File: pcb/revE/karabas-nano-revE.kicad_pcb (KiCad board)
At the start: 2 copper layers, 101.6 x 99.7 mm, 155 parts, among them J1 DC 5V, J10 PWR, J11 AVR ISP, J2 TAPE IN/OUT, J3 A/V, J4 BUS, J5 KEYBOARD, J6 BUS, J7 JTAG, J9 RGB, Q1 BC846B, SW1 RESET, SW10 8, SW11 9, SW12 0, SW13 Q, SW14 A, SW15 CS, SW16 W, SW17 S, SW18 Z, SW19 E, SW2 NMI, SW20 D, SW21 X, SW22 R, SW23 F, SW24 C, SW25 T, SW26 G, SW27 V, SW28 Y, SW29 H, SW3 1, SW30 B, SW31 U, SW32 J, SW33 N, SW34 I, SW35 K, SW36 M, SW37 O, SW38 L, SW39 SS, SW4 2, SW40 P, SW41 Enter, SW42 Space, SW5 3, SW6 4, SW7 5, SW8 6, SW9 7, U1 Z80, U13 LM1117-3.3, U2 27C512, U3 BS62LV1600, U4 ATmega8A-AU, U5 ESP-12E, U6 EPM3256ATC144, U7 MicroSD, U9 AD724, Y1 28MHz, Y3 4.43MHz, Y4 20MHz

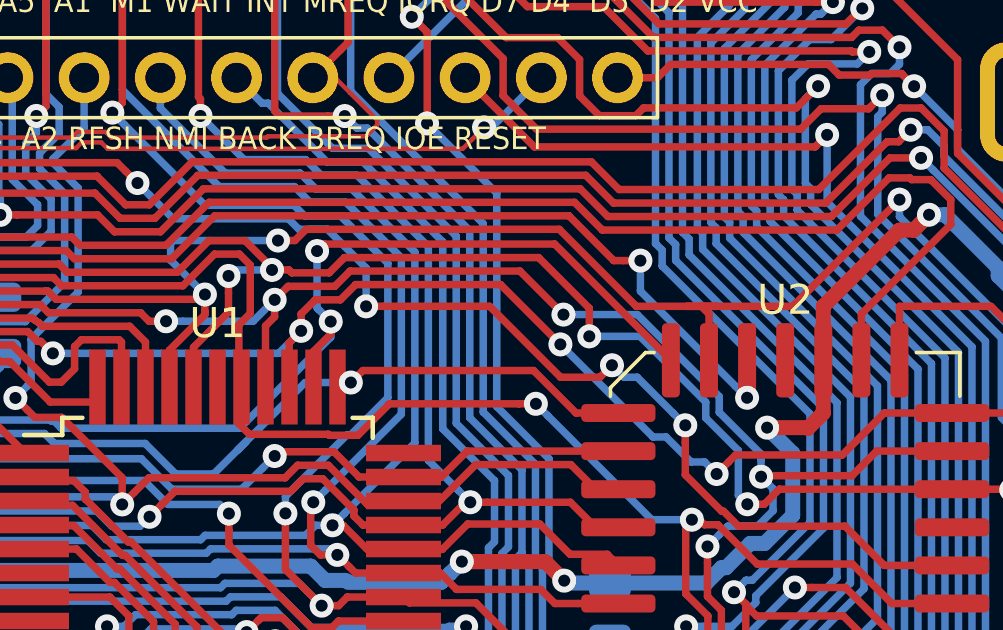
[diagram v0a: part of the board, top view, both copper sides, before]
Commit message: fixed out of sync between schematics and pcb
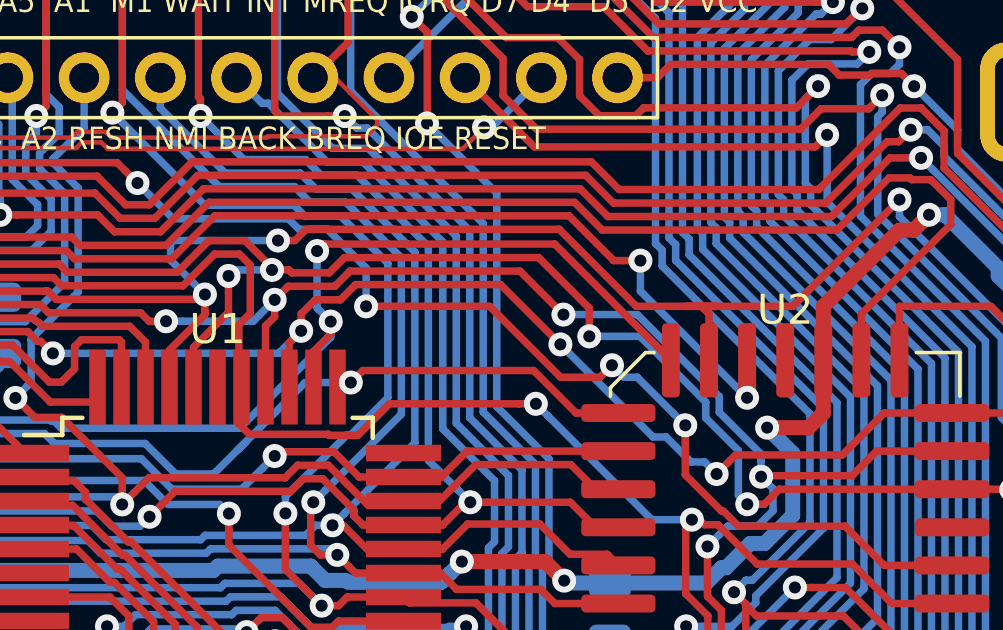
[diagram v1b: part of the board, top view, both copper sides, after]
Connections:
- SW10 pad 2: Net-(SW10-Pad2) -> /KA12
- SW10 pad 4: Net-(SW10-Pad4) -> /KB2
- SW11 pad 2: Net-(SW11-Pad2) -> /KA12
- SW11 pad 4: Net-(SW11-Pad4) -> /KB1
- SW12 pad 2: Net-(SW12-Pad2) -> /KA12
- SW12 pad 4: Net-(SW12-Pad4) -> /KB0
- SW13 pad 2: Net-(SW13-Pad2) -> /KA10
- SW13 pad 3: Net-(SW13-Pad3) -> /KB0
- SW13 pad 4: Net-(SW13-Pad4) -> /KB0
- SW14 pad 2: Net-(SW14-Pad2) -> /KA9
- SW14 pad 3: Net-(SW14-Pad3) -> /KB0
- SW14 pad 4: Net-(SW14-Pad4) -> /KB0
- SW15 pad 3: Net-(SW15-Pad3) -> /KB0
- SW15 pad 4: Net-(SW15-Pad4) -> /KB0
- SW16 pad 2: Net-(SW16-Pad2) -> /KA10
- SW16 pad 3: Net-(SW16-Pad3) -> /KB1
- SW16 pad 4: Net-(SW16-Pad4) -> /KB1
- SW17 pad 2: Net-(SW17-Pad2) -> /KA9
- SW17 pad 3: Net-(SW17-Pad3) -> /KB1
- SW17 pad 4: Net-(SW17-Pad4) -> /KB1
- SW18 pad 2: Net-(SW18-Pad2) -> /KA8
- SW18 pad 3: Net-(SW18-Pad3) -> /KB1
- SW18 pad 4: Net-(SW18-Pad4) -> /KB1
- SW19 pad 2: Net-(SW19-Pad2) -> /KA10
- SW19 pad 3: Net-(SW19-Pad3) -> /KB2
- SW19 pad 4: Net-(SW19-Pad4) -> /KB2
- SW20 pad 2: Net-(SW20-Pad2) -> /KA9
- SW20 pad 3: Net-(SW20-Pad3) -> /KB2
- SW20 pad 4: Net-(SW20-Pad4) -> /KB2
- SW21 pad 2: Net-(SW21-Pad2) -> /KA8
- SW21 pad 3: Net-(SW21-Pad3) -> /KB2
- SW21 pad 4: Net-(SW21-Pad4) -> /KB2
- SW22 pad 2: Net-(SW22-Pad2) -> /KA10
- SW22 pad 3: Net-(SW22-Pad3) -> /KB3
- SW22 pad 4: Net-(SW22-Pad4) -> /KB3
- SW23 pad 2: Net-(SW23-Pad2) -> /KA9
- SW23 pad 3: Net-(SW23-Pad3) -> /KB3
- SW23 pad 4: Net-(SW23-Pad4) -> /KB3
- SW24 pad 2: Net-(SW24-Pad2) -> /KA8
- SW24 pad 3: Net-(SW24-Pad3) -> /KB3
- SW24 pad 4: Net-(SW24-Pad4) -> /KB3
- SW25 pad 2: Net-(SW25-Pad2) -> /KA10
- SW25 pad 3: Net-(SW25-Pad3) -> /KB4
- SW25 pad 4: Net-(SW25-Pad4) -> /KB4
- SW26 pad 2: Net-(SW26-Pad2) -> /KA9
- SW26 pad 3: Net-(SW26-Pad3) -> /KB4
- SW26 pad 4: Net-(SW26-Pad4) -> /KB4
- SW27 pad 2: Net-(SW27-Pad2) -> /KA8
- SW27 pad 3: Net-(SW27-Pad3) -> /KB4
- SW27 pad 4: Net-(SW27-Pad4) -> /KB4
- SW28 pad 2: Net-(SW28-Pad2) -> /KA13
- SW28 pad 3: Net-(SW28-Pad3) -> /KB4
- SW28 pad 4: Net-(SW28-Pad4) -> /KB4
- SW29 pad 2: Net-(SW29-Pad2) -> /KA14
- SW29 pad 3: Net-(SW29-Pad3) -> /KB4
- SW29 pad 4: Net-(SW29-Pad4) -> /KB4
- SW3 pad 2: Net-(SW3-Pad2) -> /KA11
- SW3 pad 3: Net-(SW3-Pad3) -> /KB0
- SW3 pad 4: Net-(SW3-Pad4) -> /KB0
- SW30 pad 2: Net-(SW30-Pad2) -> /KA15
- SW30 pad 3: Net-(SW30-Pad3) -> /KB4
- SW30 pad 4: Net-(SW30-Pad4) -> /KB4
- SW31 pad 2: Net-(SW31-Pad2) -> /KA13
- SW31 pad 3: Net-(SW31-Pad3) -> /KB3
- SW31 pad 4: Net-(SW31-Pad4) -> /KB3
- SW32 pad 2: Net-(SW32-Pad2) -> /KA14
- SW32 pad 3: Net-(SW32-Pad3) -> /KB3
- SW32 pad 4: Net-(SW32-Pad4) -> /KB3
- SW33 pad 2: Net-(SW33-Pad2) -> /KA15
- SW33 pad 3: Net-(SW33-Pad3) -> /KB3
- SW33 pad 4: Net-(SW33-Pad4) -> /KB3
- SW34 pad 2: Net-(SW34-Pad2) -> /KA13
- SW34 pad 3: Net-(SW34-Pad3) -> /KB2
- SW34 pad 4: Net-(SW34-Pad4) -> /KB2
- SW35 pad 2: Net-(SW35-Pad2) -> /KA14
- SW35 pad 3: Net-(SW35-Pad3) -> /KB2
- SW35 pad 4: Net-(SW35-Pad4) -> /KB2
- SW36 pad 2: Net-(SW36-Pad2) -> /KA15
- SW36 pad 3: Net-(SW36-Pad3) -> /KB2
- SW36 pad 4: Net-(SW36-Pad4) -> /KB2
- SW37 pad 2: Net-(SW37-Pad2) -> /KA13
- SW37 pad 3: Net-(SW37-Pad3) -> /KB1
- SW37 pad 4: Net-(SW37-Pad4) -> /KB1
- SW38 pad 2: Net-(SW38-Pad2) -> /KA14
- SW38 pad 3: Net-(SW38-Pad3) -> /KB1
- SW38 pad 4: Net-(SW38-Pad4) -> /KB1
- SW39 pad 2: Net-(SW39-Pad2) -> /KA15
- SW39 pad 3: Net-(SW39-Pad3) -> /KB1
- SW39 pad 4: Net-(SW39-Pad4) -> /KB1
- SW4 pad 2: Net-(SW4-Pad2) -> /KA11
- SW4 pad 3: Net-(SW4-Pad3) -> /KB1
- SW4 pad 4: Net-(SW4-Pad4) -> /KB1
- SW40 pad 2: Net-(SW40-Pad2) -> /KA13
- SW40 pad 3: Net-(SW40-Pad3) -> /KB0
- SW40 pad 4: Net-(SW40-Pad4) -> /KB0
- SW41 pad 2: Net-(SW41-Pad2) -> /KA14
- SW41 pad 3: Net-(SW41-Pad3) -> /KB0
- SW41 pad 4: Net-(SW41-Pad4) -> /KB0
- SW42 pad 2: Net-(SW42-Pad2) -> /KA15
- SW42 pad 3: Net-(SW42-Pad3) -> /KB0
- SW42 pad 4: Net-(SW42-Pad4) -> /KB0
- SW5 pad 2: Net-(SW5-Pad2) -> /KA11
- SW5 pad 3: Net-(SW5-Pad3) -> /KB2
- SW5 pad 4: Net-(SW5-Pad4) -> /KB2
- SW6 pad 2: Net-(SW6-Pad2) -> /KA11
- SW6 pad 3: Net-(SW6-Pad3) -> /KB3
- SW6 pad 4: Net-(SW6-Pad4) -> /KB3
- SW7 pad 2: Net-(SW7-Pad2) -> /KA11
- SW7 pad 3: Net-(SW7-Pad3) -> /KB4
- SW7 pad 4: Net-(SW7-Pad4) -> /KB4
- SW8 pad 2: Net-(SW8-Pad2) -> /KA12
- SW8 pad 4: Net-(SW8-Pad4) -> /KB4
- SW9 pad 2: Net-(SW9-Pad2) -> /KA12
- SW9 pad 4: Net-(SW9-Pad4) -> /KB3
- U9 pad 13: Net-(U9-Pad13) -> GND
- U9 pad 14: Net-(U9-Pad14) -> VCC
- U9 pad 4: Net-(U9-Pad4) -> VCC
- Y3 pad 2: Net-(Y3-Pad2) -> Net-(C8-Pad2)
